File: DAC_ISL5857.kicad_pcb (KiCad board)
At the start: 2 copper layers, 32.8 x 39.1 mm, 21 parts, among them J1 P102, J2 P101, J3 P103, T1 1:1, U1 MIC5504-3.3, U2 ISL5857, X1 ANT

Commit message: Generate Gerber files
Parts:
- added C9: 10uF, Capacitor_SMD:C_0603_1608Metric_Pad1.05x0.95mm_HandSolder, F.Cu at (148.2, 111.0)
- added R1: 100, Resistor_SMD:R_0402_1005Metric, F.Cu at (138.5, 111.2)
- added R10: 100, Resistor_SMD:R_0402_1005Metric, F.Cu at (150.0, 116.7)
- added R11: 100, Resistor_SMD:R_0402_1005Metric, F.Cu at (138.5, 94.2)
- added R12: 100, Resistor_SMD:R_0402_1005Metric, F.Cu at (138.5, 106.2)
- added R13: 100, Resistor_SMD:R_0402_1005Metric, F.Cu at (138.5, 96.2)
- added R14: 100, Resistor_SMD:R_0402_1005Metric, F.Cu at (138.5, 108.2)
- added R15: 0, Resistor_SMD:R_0402_1005Metric, F.Cu at (149.5, 118.4)
- added R16: 22, Resistor_SMD:R_0402_1005Metric, F.Cu at (139.5, 85.2)
- added R17: 22, Resistor_SMD:R_0402_1005Metric, F.Cu at (139.5, 87.2)
- added R18: 22, Resistor_SMD:R_0402_1005Metric, F.Cu at (139.5, 89.2)
- added R19: 22, Resistor_SMD:R_0402_1005Metric, F.Cu at (139.5, 91.2)
- added R20: 22, Resistor_SMD:R_0402_1005Metric, F.Cu at (139.5, 93.2)
- added R21: 22, Resistor_SMD:R_0402_1005Metric, F.Cu at (139.5, 95.2)
- added R22: 22, Resistor_SMD:R_0402_1005Metric, F.Cu at (139.5, 97.2)
- added R23: 22, Resistor_SMD:R_0402_1005Metric, F.Cu at (139.5, 99.2)
- added R24: 22, Resistor_SMD:R_0402_1005Metric, F.Cu at (139.5, 101.2)
- added R25: 22, Resistor_SMD:R_0402_1005Metric, F.Cu at (139.5, 103.2)
- added R26: 22, Resistor_SMD:R_0402_1005Metric, F.Cu at (139.5, 105.2)
- added R27: 22, Resistor_SMD:R_0402_1005Metric, F.Cu at (139.5, 107.2)
- added R28: 22, Resistor_SMD:R_0402_1005Metric, F.Cu at (139.5, 110.2)
- added R29: 100, Resistor_SMD:R_0402_1005Metric, F.Cu at (149.0, 116.7)
- added R30: 0, Resistor_SMD:R_0603_1608Metric_Pad1.05x0.95mm_HandSolder, F.Cu at (152.7, 108.2)
- added R32: 49.9, Resistor_SMD:R_0603_1608Metric_Pad1.05x0.95mm_HandSolder, F.Cu at (152.7, 98.0)
- added R33: 120, Resistor_SMD:R_0603_1608Metric_Pad1.05x0.95mm_HandSolder, F.Cu at (153.5, 105.2)
- added R5: 100, Resistor_SMD:R_0402_1005Metric, F.Cu at (138.5, 100.2)
- added R6: 100, Resistor_SMD:R_0402_1005Metric, F.Cu at (138.5, 90.2)
- added R7: 100, Resistor_SMD:R_0402_1005Metric, F.Cu at (138.5, 102.2)
- added R8: 100, Resistor_SMD:R_0402_1005Metric, F.Cu at (138.5, 92.2)
- added R9: 100, Resistor_SMD:R_0402_1005Metric, F.Cu at (138.5, 104.2)
- added REF**: OSHW-Logo2_7.3x6mm_SilkScreen, Symbol:OSHW-Logo2_7.3x6mm_SilkScreen, F.Cu at (146.6, 87.8)
- added X2: ANT, Connector_Coaxial:SMA_Molex_73251-1153_EdgeMount_Horizontal, F.Cu at (157.6, 89.7)
- C3, C8: value 10uF -> 0.1uF
- C4: value 0.1uF -> 10uF
- J3: footprint Connector_PinHeader_1.00mm:PinHeader_1x03_P1.00mm_Vertical -> Connector_PinHeader_2.54mm:PinHeader_1x03_P2.54mm_Vertical
- R2: value 49.9 -> 100; footprint Resistor_SMD:R_0603_1608Metric_Pad1.05x0.95mm_HandSolder -> Resistor_SMD:R_0402_1005Metric
- R3: value 120 -> 100; footprint Resistor_SMD:R_0603_1608Metric_Pad1.05x0.95mm_HandSolder -> Resistor_SMD:R_0402_1005Metric
- R4: value 1.8K -> 100; footprint Resistor_SMD:R_0603_1608Metric_Pad1.05x0.95mm_HandSolder -> Resistor_SMD:R_0402_1005Metric
- X1: value ANT -> ASFL1; footprint Connector_Coaxial:SMA_Molex_73251-1153_EdgeMount_Horizontal -> Oscillator:Oscillator_SMD_Abracon_ASE-4Pin_3.2x2.5mm
- moved C3 31.8 mm to (157.2, 117.6), turned to 90 degrees
- moved X1 28.3 mm to (153.8, 117.6)
- moved R2 18.8 mm to (138.5, 86.2), turned to 180 degrees
- moved L1 17.6 mm to (143.8, 109.3)
- moved C4 17.6 mm to (143.8, 111.0), turned to 0 degrees
- moved L2 17.4 mm to (148.2, 109.3)
- moved R3 16.5 mm to (138.5, 98.2)
- moved C8 15.5 mm to (151.5, 105.2), turned to 90 degrees
- moved C5 14.6 mm to (143.8, 107.5), turned to 180 degrees
- moved T1 9.08 mm to (152.7, 93.0), turned to 180 degrees
- moved R4 8.81 mm to (138.5, 88.2), turned to 180 degrees
- moved C7 8.60 mm to (158.1, 100.0), turned to 90 degrees
- moved C6 4.29 mm to (148.2, 107.5), turned to 0 degrees
- moved R31 3.85 mm to (152.7, 102.4)
- moved U2 3.40 mm to (146.0, 100.1)
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- renumbered R1 to R31
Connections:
- C4 pad 2: Net-(C4-Pad2) -> +3V3
- C5 pad 2: Net-(C5-Pad2) -> /DVDD
- C6 pad 2: Net-(C6-Pad2) -> /AVDD
- C8 pad 2: +3V3 -> Net-(C8-Pad2)
- J1 pad 5: Net-(J1-Pad5) -> /CLK
- J1 pad 6: Net-(J1-Pad6) -> /PD
- J1 pad 8: /CLK -> SYS_MCLK
- L1 pad 1: Net-(C4-Pad2) -> /DVDD
- L2 pad 2: Net-(C5-Pad2) -> /AVDD
- R2 pad 1: /RF_P -> /D11
- R2 pad 2: /RF_N -> GND
- R3 pad 2: Net-(R1-Pad1) -> /D5
- R31 pad 1: Net-(R1-Pad1) -> Net-(R31-Pad1)
- R4 pad 1: /D11 -> /D10
- U2 pad 1: /D11 -> Net-(R16-Pad1)
- U2 pad 10: /D2 -> Net-(R25-Pad1)
- U2 pad 11: /D1 -> Net-(R26-Pad1)
- U2 pad 12: /D0 -> Net-(R27-Pad1)
- U2 pad 15: GND -> /PD
- U2 pad 17: Net-(C6-Pad2) -> Net-(C8-Pad2)
- U2 pad 2: /D10 -> Net-(R17-Pad1)
- U2 pad 24: Net-(C5-Pad2) -> /AVDD
- U2 pad 27: Net-(C4-Pad2) -> /DVDD
- U2 pad 28: /CLK -> Net-(R28-Pad1)
- U2 pad 3: /D9 -> Net-(R18-Pad1)
- U2 pad 4: /D8 -> Net-(R19-Pad1)
- U2 pad 5: /D7 -> Net-(R20-Pad1)
- U2 pad 6: /D6 -> Net-(R21-Pad1)
- U2 pad 7: /D5 -> Net-(R22-Pad1)
- U2 pad 8: /D4 -> Net-(R23-Pad1)
- U2 pad 9: /D3 -> Net-(R24-Pad1)
- X1 pad 1: Net-(T1-Pad4) -> +3V3
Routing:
- net /PD: track 0.00 -> 24.5 mm, vias 0 -> 2
- net GND: track 18.1 -> 40.8 mm, vias 0 -> 17
- net Net-(R28-Pad1): track 0.00 -> 21.1 mm, vias 0 -> 1
- net SYS_MCLK: track 0.00 -> 19.4 mm, vias 0 -> 2
- net Net-(R16-Pad1): track 0.00 -> 11.9 mm
- net /D3: track 0.00 -> 11.5 mm
- net Net-(R17-Pad1): track 0.00 -> 11.1 mm
- net /D1: track 0.00 -> 10.4 mm
- net Net-(C5-Pad2): track 10.4 -> 0.00 mm
- net /D4: track 3.97 -> 14.1 mm
- net /D5: track 0.68 -> 10.6 mm
- net Net-(R18-Pad1): track 0.00 -> 9.74 mm
- net /CLK: track 0.00 -> 9.33 mm
- net /D6: track 3.62 -> 12.7 mm
- net /D7: track 0.54 -> 8.97 mm
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- added copper zone on In2.Cu, net +3V3
- added copper zone on In2.Cu, net /AVDD
- added copper zone on In2.Cu, net /DVDD
- added copper zone on In1.Cu, net GND
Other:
- copper layers 2 -> 4
- net class 50ohm added: clearance 0.1524, trace_width 0.3048, via_dia 0.508, via_drill 0.254
- net class RF removed
- board text added: "+5V"
- board text added: "GND"
- board text added: "TXDAC_12 Rev. A HB9GPC"
- board text added: "VDD"

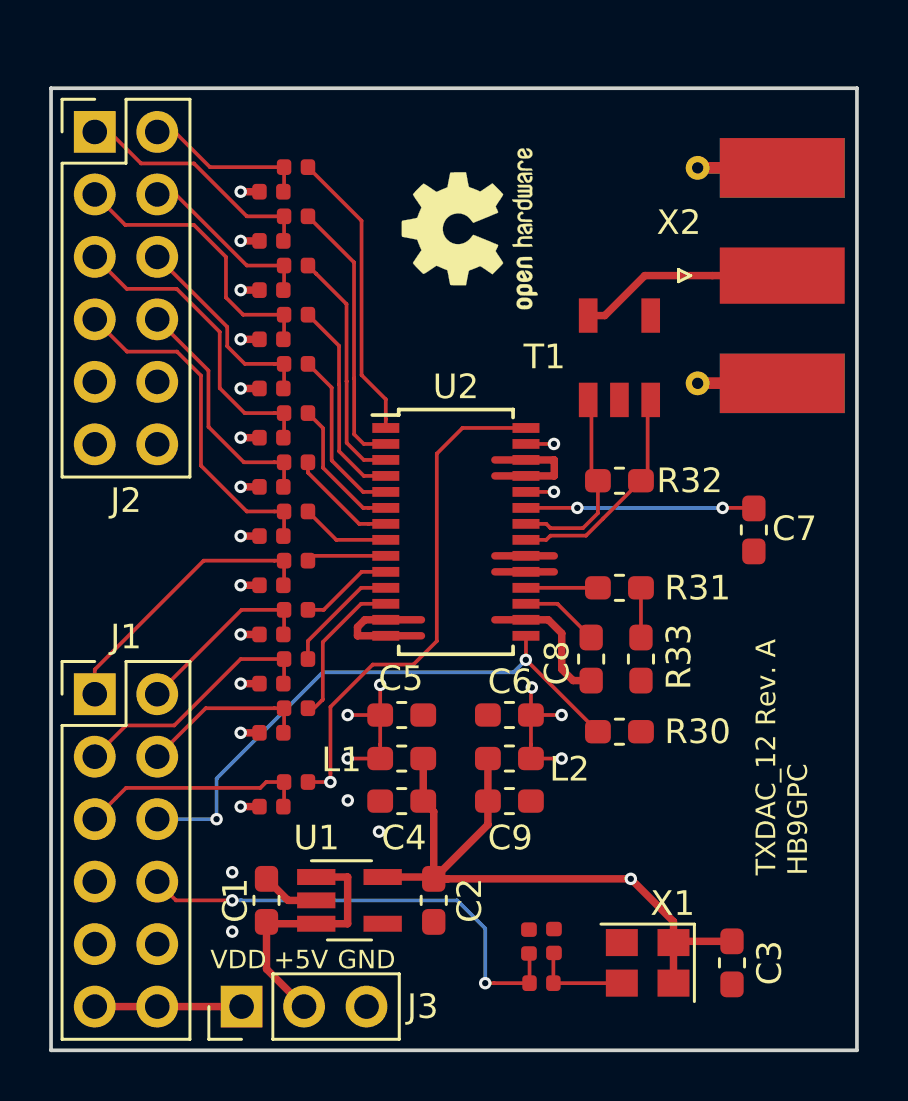
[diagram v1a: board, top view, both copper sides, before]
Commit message: Replace IC reg linear and clock footprint
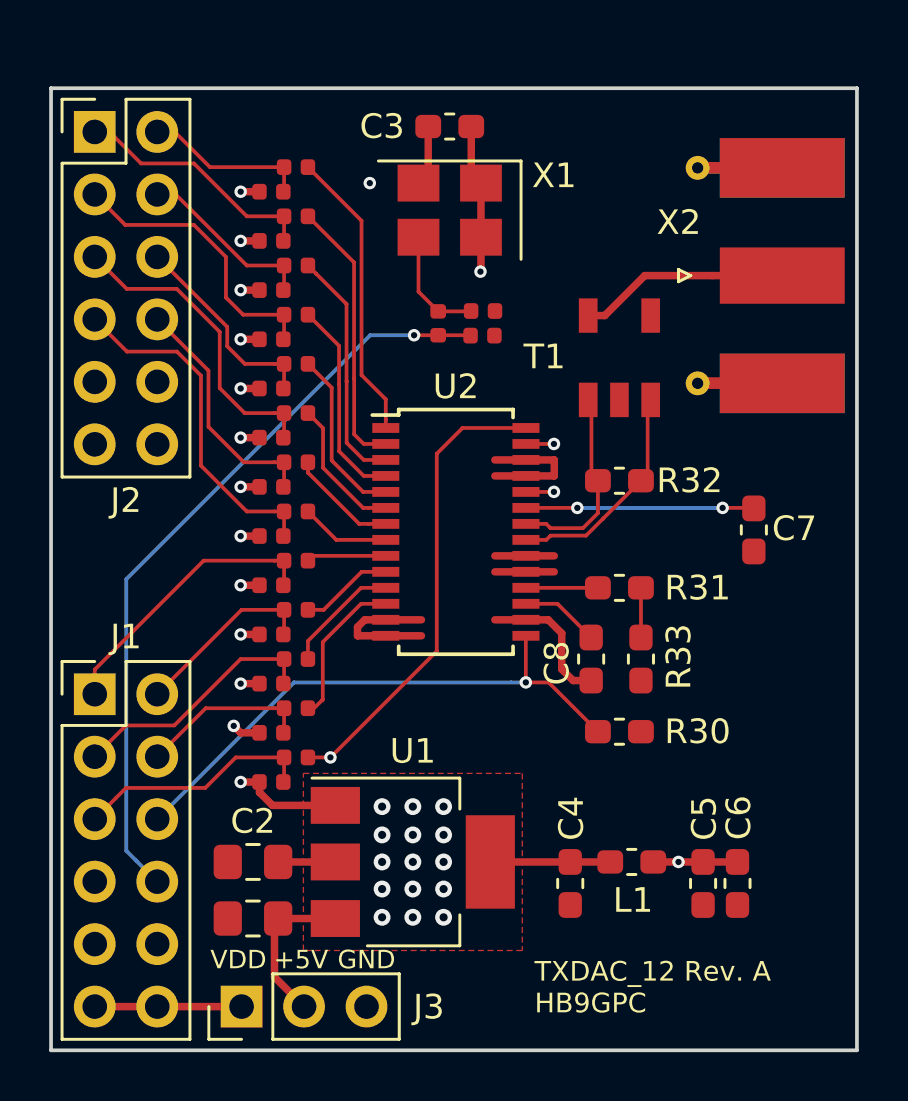
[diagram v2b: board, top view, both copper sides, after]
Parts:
- removed C9: 10uF, Capacitor_SMD:C_0603_1608Metric_Pad1.05x0.95mm_HandSolder
- removed L2: 10uH, Inductor_SMD:L_0603_1608Metric_Pad1.05x0.95mm_HandSolder
- removed the REF** at (146.6, 87.8)
- added REF**: OSHW-Logo2_9.8x8mm_SilkScreen, Symbol:OSHW-Logo2_9.8x8mm_SilkScreen, B.Cu at (144.0, 100.2)
- C1, C2: value 1uF -> 10uF; footprint Capacitor_SMD:C_0603_1608Metric_Pad1.05x0.95mm_HandSolder -> Capacitor_SMD:C_0805_2012Metric_Pad1.15x1.40mm_HandSolder
- C4: value 10uF -> 0.1uF
- C6: value 0.1uF -> 10uF
- U1: value MIC5504-3.3 -> LD1117S33CTR; footprint Package_TO_SOT_SMD:SOT-23-5_HandSoldering -> Package_TO_SOT_SMD:SOT-223-3_TabPin2
- X1: footprint Oscillator:Oscillator_SMD_Abracon_ASE-4Pin_3.2x2.5mm -> DRA818:Crystal_SMD_Abracon_ASFL1-4pin_5.0x3.2mm
- moved C3 35.9 mm to (145.8, 83.6), turned to 0 degrees
- moved X1 31.6 mm to (145.8, 87.0)
- moved R15 27.2 mm to (145.3, 91.6), turned to 90 degrees
- moved R10 25.8 mm to (147.1, 91.1), turned to 180 degrees
- moved R29 24.7 mm to (147.1, 92.1), turned to 180 degrees
- moved C5 14.0 mm to (156.1, 114.4), turned to 90 degrees
- moved C6 11.5 mm to (157.4, 114.4), turned to 90 degrees
- moved L1 10.3 mm to (153.2, 113.5), turned to 180 degrees
- moved C4 7.63 mm to (150.7, 114.4), turned to 90 degrees
- moved C2 7.51 mm to (137.8, 113.5), turned to 0 degrees
- moved U1 3.01 mm to (144.2, 113.5)
- moved R1 1.00 mm to (138.5, 110.2)
- moved R28 1.00 mm to (139.5, 109.2)
- moved C1 0.92 mm to (137.8, 115.8), turned to 0 degrees
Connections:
- C5 pad 2: /DVDD -> +3.3VADC
- C6 pad 2: /AVDD -> +3.3VADC
- J1 pad 7: Net-(J1-Pad7) -> (no net)
- J2 pad 11: Net-(J2-Pad11) -> (no net)
- J2 pad 12: Net-(J2-Pad12) -> (no net)
- L1 pad 1: /DVDD -> +3.3VADC
- U1 pad 1: +5V -> GND
- U1 pad 2: GND -> +3V3
- U2 pad 24: /AVDD -> +3.3VADC
- U2 pad 27: /DVDD -> +3V3
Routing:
- net +3V3: track 28.8 -> 14.6 mm, vias 1 -> 17
- net SYS_MCLK: track 19.4 -> 30.9 mm, vias 2 -> 1
- net /DVDD: track 6.78 -> 0.00 mm, vias 4 -> 0
- net /AVDD: track 6.54 -> 0.00 mm, vias 4 -> 0
- net +3.3VADC: track 0.00 -> 4.56 mm, vias 0 -> 2
- net GND: track 40.8 -> 45.0 mm, vias 17 -> 14
- net +5V: track 10.6 -> 6.55 mm
- net Net-(R28-Pad1): track 21.1 -> 19.1 mm
- net /PD: track 24.5 -> 22.9 mm, vias 2 -> 1
- net Net-(R10-Pad2): track 4.02 -> 4.69 mm
- added copper zone on In2.Cu, net +3.3VADC
- added copper zone on F.Cu, net +3V3
- removed copper zone on In2.Cu, net /AVDD
- removed copper zone on In2.Cu, net /DVDD
